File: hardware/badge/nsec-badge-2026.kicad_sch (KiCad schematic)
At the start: 0 parts

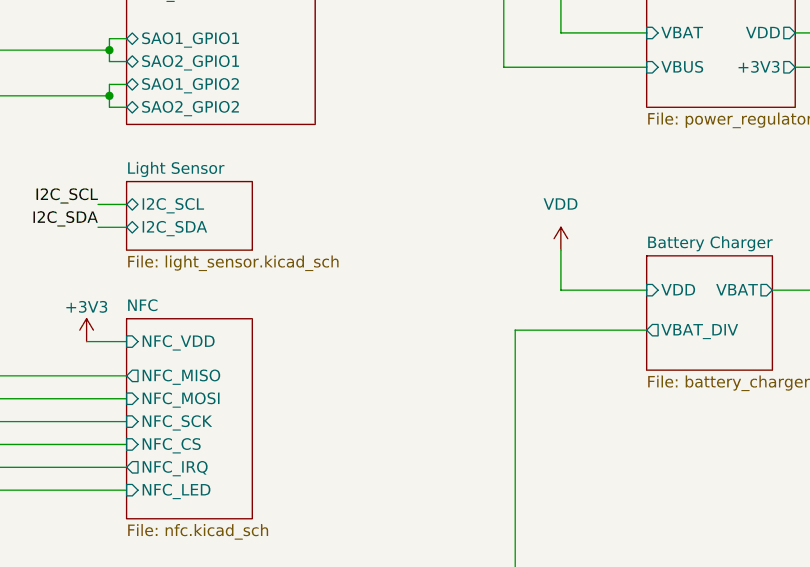
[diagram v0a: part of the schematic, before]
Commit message: feat: badge v2 PCB design with panelization support
Updated schematic and PCB layout for badge v2 revision. Added
panelization project with JLCPCB production files, panelize script,
and board SVG artwork.
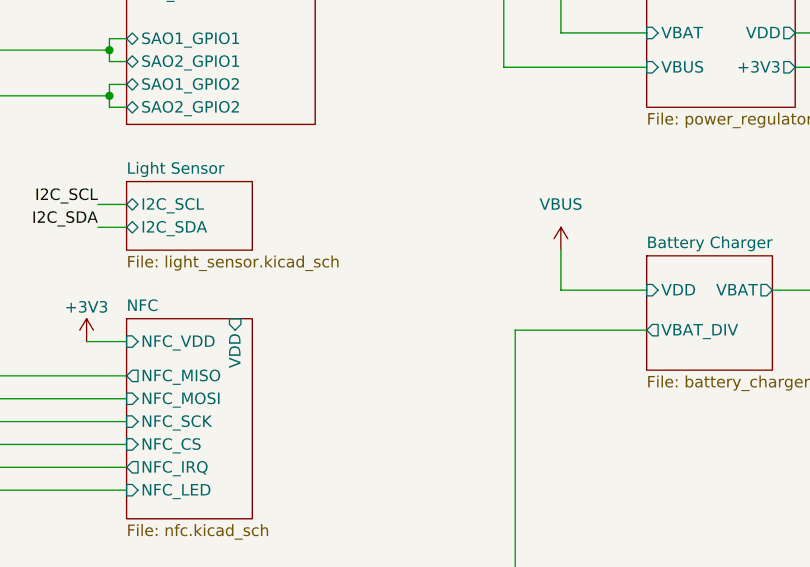
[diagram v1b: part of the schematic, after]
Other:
- sheet NFC ports: added VDD; removed none
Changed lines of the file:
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@@
+	)
+	(symbol
+		(lib_id "power:VBUS")
+		(at 212.725 109.855 0)
+		(mirror y)
+		(unit 1)
+		(exclude_from_sim no)
+		(in_bom yes)
+		(on_board yes)
+		(dnp no)
+		(property "Reference" "#PWR0104"
+			(at 212.725 113.665 0)
+			(effects
+				(font
+					(size 1.27 1.27)
+				)
+				(hide yes)
+			)
+		)
+		(property "Value" "VBUS"
+			(at 212.725 104.775 0)
+			(effects
+				(font
+					(size 1.27 1.27)
+				)
+			)
+		)
+		(property "Footprint" ""
+			(at 212.725 109.855 0)
+			(effects
+				(font
+					(size 1.27 1.27)
+				)
+				(hide yes)
+			)
+		)
+		(property "Datasheet" ""
+			(at 212.725 109.855 0)
+			(effects
+				(font
+					(size 1.27 1.27)
+				)
+				(hide yes)
+			)
+		)
+		(property "Description" "Power symbol creates a global label with name \"VBUS\""
+			(at 212.725 109.855 0)
+			(effects
+				(font
+					(size 1.27 1.27)
+				)
+				(hide yes)
+			)
+		)
+		(pin "1"
+		)
+		(instances
+			(project "nsec-badge-2026"
+				(path "/4058d5ec-aa3f-4b7a-8f79-61676c76e695"
+					(reference "#PWR0104")
+					(unit 1)
+				)
+			)
+		)
 	)
 	(symbol
@@
 		)
 	)
-	(symbol
-		(lib_id "power:VDD")
-		(at 212.725 109.855 0)
-		(unit 1)
-		(exclude_from_sim no)
-		(in_bom yes)
-		(on_board yes)
-		(dnp no)
-		(fields_autoplaced yes)
-		(property "Reference" "#PWR0104"
-			(at 212.725 113.665 0)
-			(effects
-				(font
-					(size 1.27 1.27)
-				)
-				(hide yes)
-			)
-		)
-		(property "Value" "VDD"
-			(at 212.725 104.775 0)
-			(effects
-				(font
-					(size 1.27 1.27)
-				)
-			)
-		)
-		(property "Footprint" ""
-			(at 212.725 109.855 0)
-			(effects
-				(font
-					(size 1.27 1.27)
-				)
-				(hide yes)
-			)
-		)
-		(property "Datasheet" ""
-			(at 212.725 109.855 0)
-			(effects
-				(font
-					(size 1.27 1.27)
-				)
-				(hide yes)
-			)
-		)
-		(property "Description" "Power symbol creates a global label with name \"VDD\""
-			(at 212.725 109.855 0)
-			(effects
-				(font
-					(size 1.27 1.27)
-				)
-				(hide yes)
-			)
-		)
-		(pin "1"
-		)
-		(instances
-			(project "nsec-badge-2026"
-				(path "/4058d5ec-aa3f-4b7a-8f79-61676c76e695"
-					(reference "#PWR0104")
-					(unit 1)
-				)
-			)
-		)
-	)
 	(sheet
 		(at 164.465 60.96)
@@
 			)
 		)
+		(pin "VDD" input
+			(at 176.53 117.475 90)
+			(effects
+				(font
+					(size 1.27 1.27)
+				)
+				(justify right)
+			)
+		)
